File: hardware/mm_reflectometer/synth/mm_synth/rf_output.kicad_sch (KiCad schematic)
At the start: 40 parts

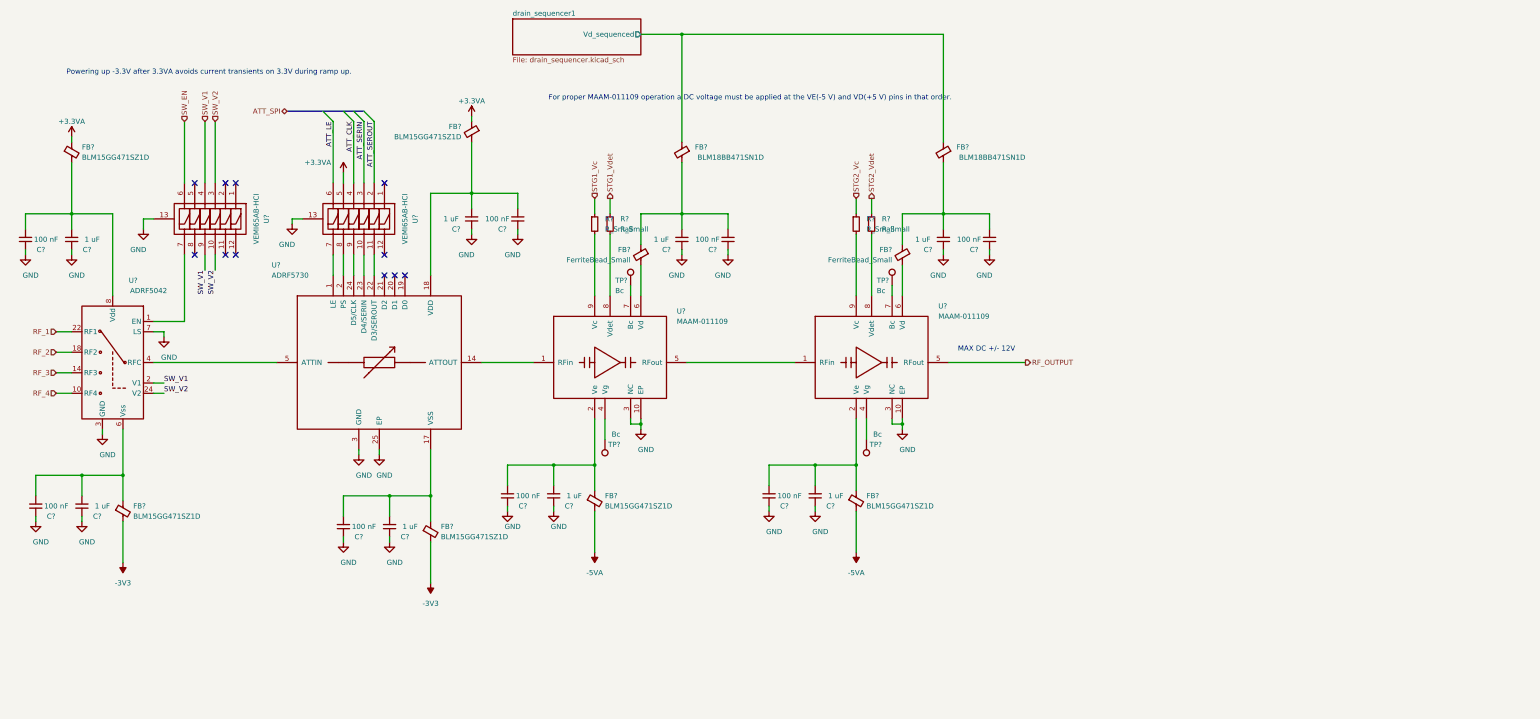
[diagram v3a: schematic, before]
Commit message: work on mm synth schematic - control signals and footprint assignments
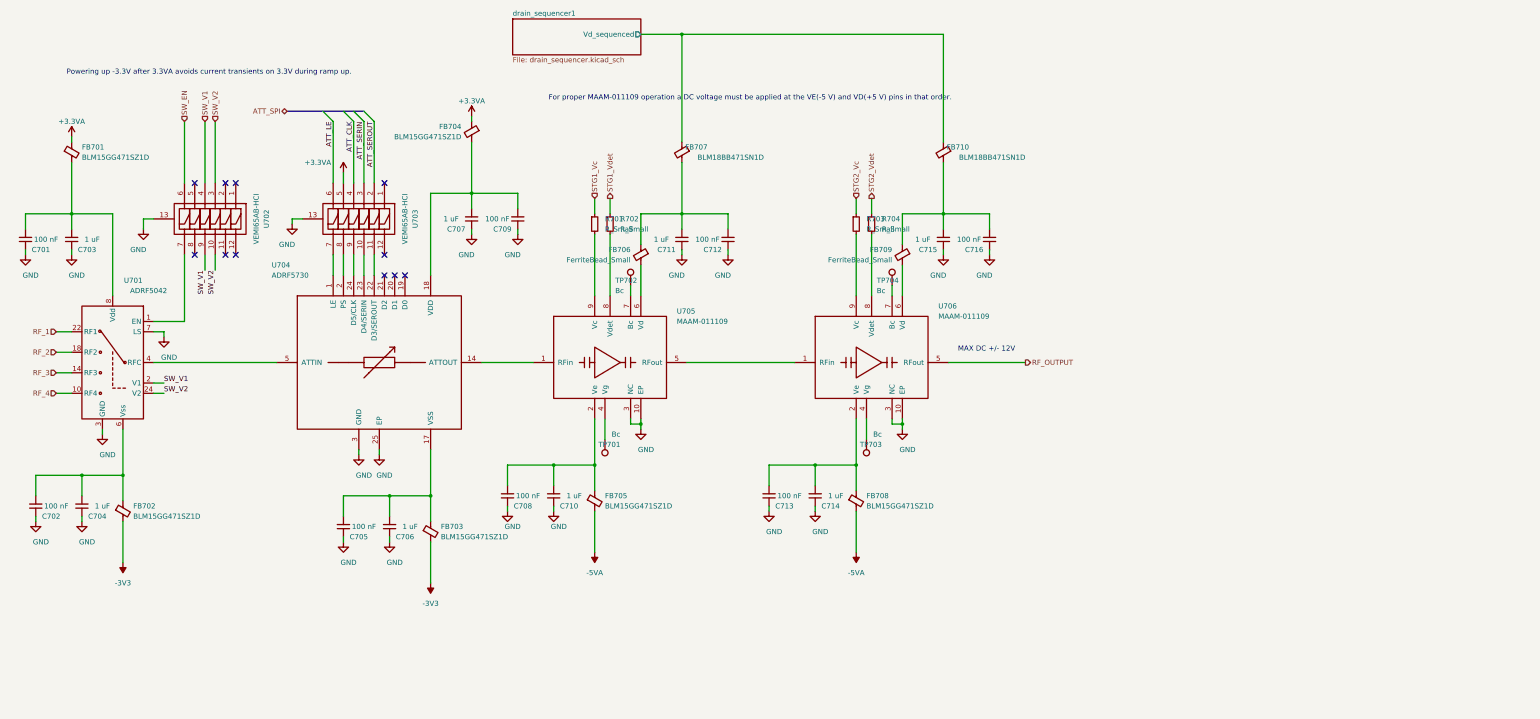
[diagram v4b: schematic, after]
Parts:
- C701, C702, C703, C704, C705, C706, C707, C708, C709, C710, C711, C712, C713, C714, C715, C716: renamed from C?; footprint (none) -> Capacitor_SMD:C_0402_1005Metric
- R701, R702, R703, R704: renamed from R?; footprint (none) -> Resistor_SMD:R_0402_1005Metric
- TP701, TP702, TP703, TP704: renamed from TP?; footprint (none) -> TestPoint:TestPoint_Pad_D1.5mm
- U702, U703: renamed from U?; footprint (none) -> vna_mm:LLP2513-13L
- gave numbers to parts that had none: 14

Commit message: added aux high speed io connector, fixed hierarchical buses
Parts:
- FB701, FB702, FB703, FB704, FB705, FB708: footprint (none) -> Inductor_SMD:L_0402_1005Metric
- FB706, FB709: value FerriteBead_Small -> BLM18BB471SN1D; footprint (none) -> Inductor_SMD:L_0603_1608Metric
- FB707, FB710: footprint (none) -> Inductor_SMD:L_0603_1608Metric
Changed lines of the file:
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@@
   (no_connect (at 110.49 86.36))
   (no_connect (at 113.03 86.36))
-  (bus_entry (at 92.71 45.72) (size 2.54 2.54)
-    (stroke (width 0.1524) (type solid) (color 0 0 0 0))
-  )
-  (bus_entry (at 97.79 45.72) (size 2.54 2.54)
-    (stroke (width 0.1524) (type solid) (color 0 0 0 0))
-  )
-  (bus_entry (at 100.33 45.72) (size 2.54 2.54)
-    (stroke (width 0.1524) (type solid) (color 0 0 0 0))
-  )
-  (bus_entry (at 102.87 45.72) (size 2.54 2.54)
-    (stroke (width 0.1524) (type solid) (color 0 0 0 0))
-  )
   (wire (pts (xy 19.05 71.12) (xy 30.48 71.12))
     (stroke (width 0) (type solid) (color 0 0 0 0))
@@
   )
   (wire (pts (xy 257.81 80.01) (xy 257.81 81.28))
-    (stroke (width 0) (type solid) (color 0 0 0 0))
-  )
-  (bus (pts (xy 83.82 45.72) (xy 102.87 45.72))
     (stroke (width 0) (type solid) (color 0 0 0 0))
   )
@@
     (effects (font (size 1.27 1.27)) (justify right bottom))
   )
-  (label "ATT_LE" (at 95.25 48.26 270)
-    (effects (font (size 1.27 1.27)) (justify right bottom))
-  )
-  (label "ATT_CLK" (at 100.33 48.26 270)
-    (effects (font (size 1.27 1.27)) (justify right bottom))
-  )
-  (label "ATT_SERIN" (at 102.87 48.26 270)
-    (effects (font (size 1.27 1.27)) (justify right bottom))
-  )
-  (label "ATT_SEROUT" (at 105.41 48.26 270)
-    (effects (font (size 1.27 1.27)) (justify right bottom))
-  )
   (hierarchical_label "RF_1" (shape input) (at 26.67 100.33 180)
     (effects (font (size 1.27 1.27)) (justify right))
@@
     (effects (font (size 1.27 1.27)) (justify left))
   )
-  (hierarchical_label "ATT_SPI" (shape bidirectional) (at 83.82 45.72 180)
-    (effects (font (size 1.27 1.27)) (justify right))
+  (hierarchical_label "ATT_LE" (shape input) (at 95.25 48.26 90)
+    (effects (font (size 1.27 1.27)) (justify left))
+  )
+  (hierarchical_label "ATT_CLK" (shape input) (at 100.33 48.26 90)
+    (effects (font (size 1.27 1.27)) (justify left))
+  )
+  (hierarchical_label "ATT_SERIN" (shape input) (at 102.87 48.26 90)
+    (effects (font (size 1.27 1.27)) (justify left))
+  )
+  (hierarchical_label "ATT_SEROUT" (shape output) (at 105.41 48.26 90)
+    (effects (font (size 1.27 1.27)) (justify left))
   )
   (hierarchical_label "STG1_Vc" (shape input) (at 160.02 67.31 90)
@@
       (effects (font (size 1.27 1.27)) (justify left))
     )
-    (property "Footprint" "" (id 2) (at 28.702 55.88 90)
+    (property "Footprint" "Inductor_SMD:L_0402_1005Metric" (id 2) (at 28.702 55.88 90)
       (effects (font (size 1.27 1.27)) hide)
     )
@@
       (effects (font (size 1.27 1.27)) (justify left))
     )
-    (property "Footprint" "" (id 2) (at 41.402 144.78 90)
+    (property "Footprint" "Inductor_SMD:L_0402_1005Metric" (id 2) (at 41.402 144.78 90)
       (effects (font (size 1.27 1.27)) hide)
     )
@@
       (effects (font (size 1.27 1.27)) (justify left))
     )
-    (property "Footprint" "" (id 2) (at 117.602 149.86 90)
+    (property "Footprint" "Inductor_SMD:L_0402_1005Metric" (id 2) (at 117.602 149.86 90)
       (effects (font (size 1.27 1.27)) hide)
     )
@@
       (effects (font (size 1.27 1.27)) (justify left))
     )
-    (property "Footprint" "" (id 2) (at 131.318 50.8 90)
+    (property "Footprint" "Inductor_SMD:L_0402_1005Metric" (id 2) (at 131.318 50.8 90)
       (effects (font (size 1.27 1.27)) hide)
     )
@@
       (effects (font (size 1.27 1.27)) (justify left))
     )
-    (property "Footprint" "" (id 2) (at 158.242 142.24 90)
+    (property "Footprint" "Inductor_SMD:L_0402_1005Metric" (id 2) (at 158.242 142.24 90)
       (effects (font (size 1.27 1.27)) hide)
     )
@@
       (effects (font (size 1.27 1.27)) (justify left))
     )
-    (property "Value" "FerriteBead_Small" (id 1) (at 168.91 82.55 0)
-      (effects (font (size 1.27 1.27)) (justify left))
-    )
-    (property "Footprint" "" (id 2) (at 173.228 81.28 90)
+    (property "Value" "BLM18BB471SN1D" (id 1) (at 168.91 82.55 0)
+      (effects (font (size 1.27 1.27)) (justify left))
+    )
+    (property "Footprint" "Inductor_SMD:L_0603_1608Metric" (id 2) (at 173.228 81.28 90)
       (effects (font (size 1.27 1.27)) hide)
     )
@@
       (effects (font (size 1.27 1.27)) (justify left))
     )
-    (property "Footprint" "" (id 2) (at 183.388 55.88 90)
+    (property "Footprint" "Inductor_SMD:L_0603_1608Metric" (id 2) (at 183.388 55.88 90)
       (effects (font (size 1.27 1.27)) hide)
     )
@@
       (effects (font (size 1.27 1.27)) (justify left))
     )
-    (property "Footprint" "" (id 2) (at 223.012 142.24 90)
+    (property "Footprint" "Inductor_SMD:L_0402_1005Metric" (id 2) (at 223.012 142.24 90)
       (effects (font (size 1.27 1.27)) hide)
     )
@@
       (effects (font (size 1.27 1.27)) (justify left))
     )
-    (property "Value" "FerriteBead_Small" (id 1) (at 233.68 82.55 0)
-      (effects (font (size 1.27 1.27)) (justify left))
-    )
-    (property "Footprint" "" (id 2) (at 237.998 81.28 90)
+    (property "Value" "BLM18BB471SN1D" (id 1) (at 233.68 82.55 0)
+      (effects (font (size 1.27 1.27)) (justify left))
+    )
+    (property "Footprint" "Inductor_SMD:L_0603_1608Metric" (id 2) (at 237.998 81.28 90)
       (effects (font (size 1.27 1.27)) hide)
     )
@@
       (effects (font (size 1.27 1.27)) (justify left))
     )
-    (property "Footprint" "" (id 2) (at 248.158 55.88 90)
-      (effects (font (size 1.27 1.27)) hide)
-    )
+    (property "Footprint" "Inductor_SMD:L_0603_1608Metric" (id 2) (at 248.158 55.88 90)
+      (effects (font (size 1.27 1.27)) hide)
+    )

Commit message: schematic cleanup, erc
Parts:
- TP701: value Bc -> Vg1
- TP702: value Bc -> Bc1
- TP703: value Bc -> Vg2
- TP704: value Bc -> Bc2
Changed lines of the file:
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@@
       (effects (font (size 1.27 1.27)) (justify left))
     )
-    (property "Value" "Bc" (id 1) (at 166.37 125.73 0)
+    (property "Value" "Vg1" (id 1) (at 166.37 125.73 0)
       (effects (font (size 1.27 1.27)) (justify left))
     )
@@
       (effects (font (size 1.27 1.27)) (justify left))
     )
-    (property "Value" "Bc" (id 1) (at 165.1 90.17 0)
+    (property "Value" "Bc1" (id 1) (at 165.1 90.17 0)
       (effects (font (size 1.27 1.27)) (justify left))
     )
@@
       (effects (font (size 1.27 1.27)) (justify left))
     )
-    (property "Value" "Bc" (id 1) (at 231.14 125.73 0)
+    (property "Value" "Vg2" (id 1) (at 231.14 125.73 0)
       (effects (font (size 1.27 1.27)) (justify left))
     )
@@
       (effects (font (size 1.27 1.27)) (justify left))
     )
-    (property "Value" "Bc" (id 1) (at 229.87 90.17 0)
+    (property "Value" "Bc2" (id 1) (at 229.87 90.17 0)
       (effects (font (size 1.27 1.27)) (justify left))
     )

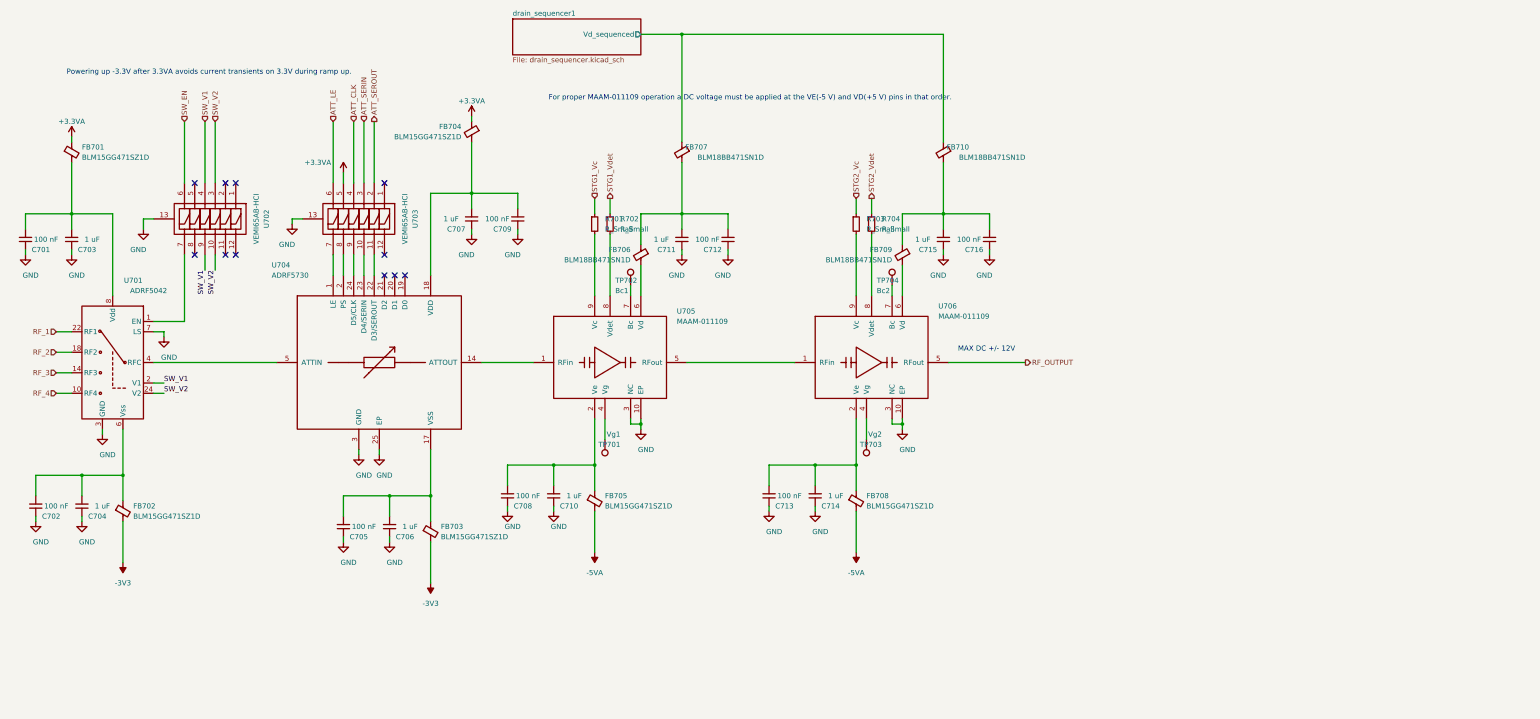
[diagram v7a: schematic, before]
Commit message: created HUSB238 eval board, added clock splitter to mm synth
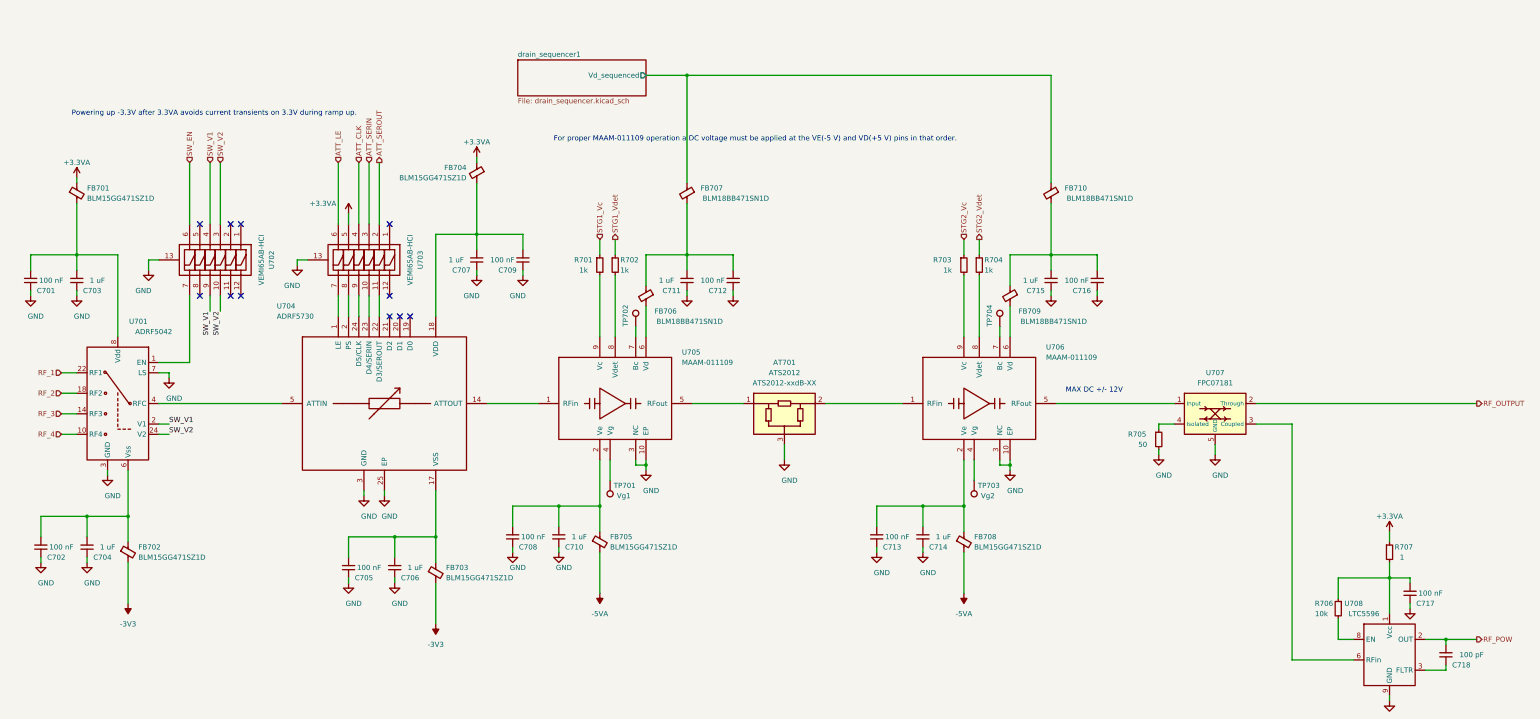
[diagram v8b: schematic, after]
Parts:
- added AT701: ATS2012, jtk_rf_footprints:ATS2012, symbol jtk_rf:ATS2012
- added C717: 100 nF, Capacitor_SMD:C_0402_1005Metric, symbol Device:C_Small
- added C718: 100 pF, Capacitor_SMD:C_0402_1005Metric, symbol Device:C_Small
- added R705: 50, Resistor_SMD:R_0402_1005Metric, symbol Device:R_Small
- added R706: 10k, Resistor_SMD:R_0402_1005Metric, symbol Device:R_Small
- added R707: 1, Resistor_SMD:R_0402_1005Metric, symbol Device:R_Small
- added U707: FPC07181, jtk_rf_footprints:FPC07181, symbol jtk_rf:FPC07181
- added U708: LTC5596, jtk_rf_footprints:DFN-8-1EP_2x2mm_P0.5mm_EP0.25x1.6mm, symbol jtk_rf:LTC5596
- R701, R702, R703, R704: value R_Small -> 1k
- TP701, TP702, TP703, TP704: now left out of the parts list
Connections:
- net +3.3VA: now also R707.1
- net GND: now also AT701.3, C717.1, R705.2, U707.5 (GND), U708.4 (GND), U708.5 (GND), U708.7 (GND), U708.9 (GND)
- net RF_OUTPUT: now also U707.2 (Through); no longer U706.5 (RFout)
- net at U705.5 (RFout): now also AT701.1; no longer U706.1 (RFin)
- new net: C717.2, R706.1, R707.2, U708.1 (Vcc)
- new net: C718.1, U708.3 (FLTR)
- new net: U707.3 (Coupled), U708.6 (RFin)
- new net: R706.2, U708.8 (EN)
- new net: AT701.2, U706.1 (RFin)
- new net: R705.1, U707.4 (Isolated)
- new net: U706.5 (RFout), U707.1 (Input)
- new net RF_POW: C718.2, U708.2 (OUT)
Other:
- moved on the sheet: C701, C702, C703, C704, C705, C706, C707, C708, C709, C710, C711, C712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
